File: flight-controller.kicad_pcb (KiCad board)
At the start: 2 copper layers, 51 x 54 mm, 32 parts, among them J1 XT60PW-M, J2 SM04B-SRSS-TB, J3 XT60PW-F, J4 XT60PW-F, J5 XT60PW-F, J6 XT60PW-F, U1 ACS773LCB-100B-PFF, U2 LMR33630ADDA, U3 AMS1117-3.3

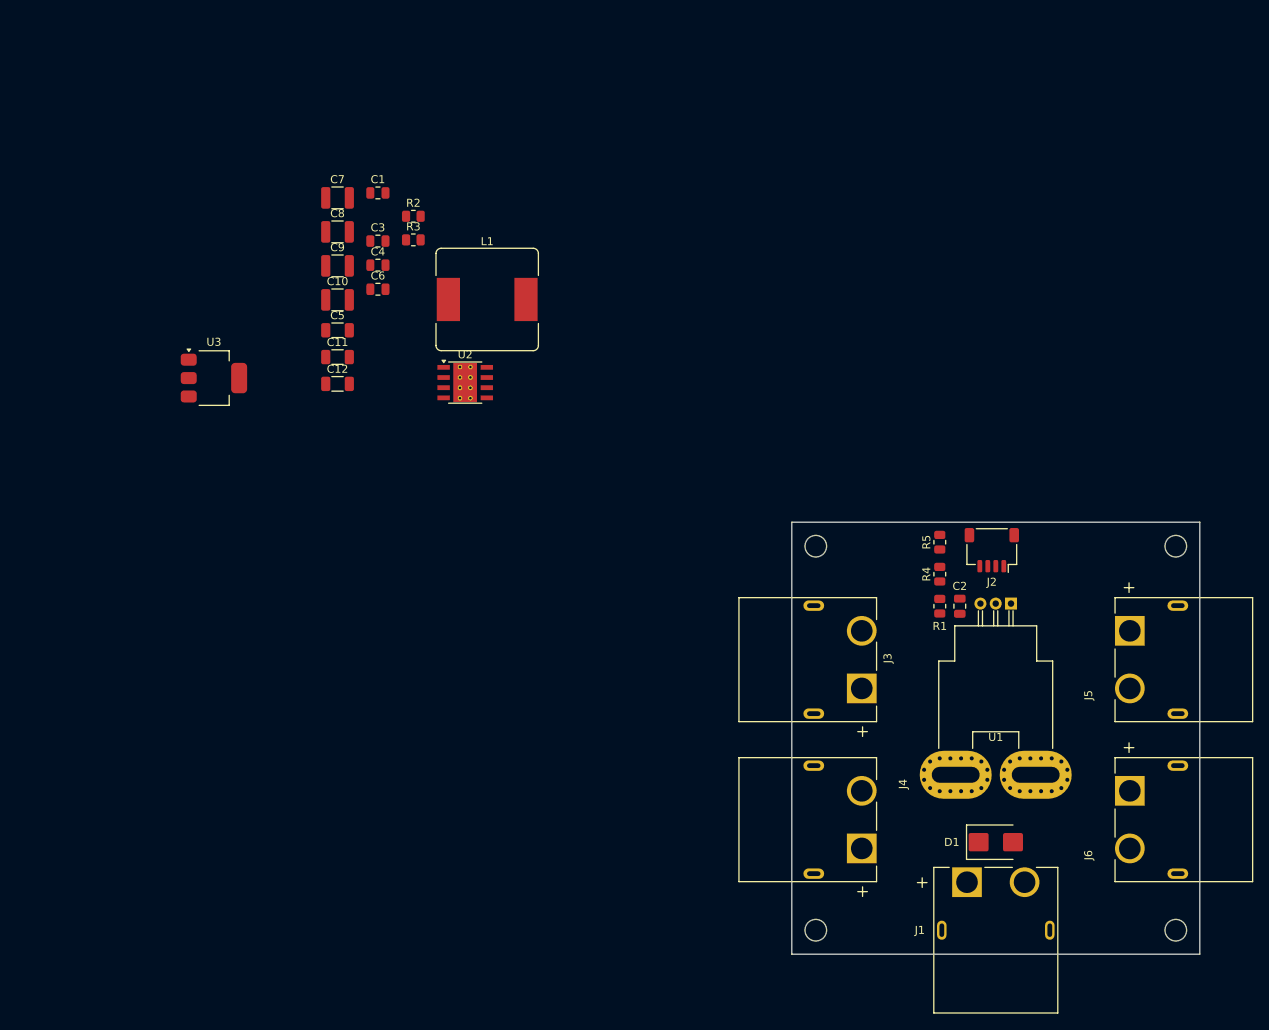
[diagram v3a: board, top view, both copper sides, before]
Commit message: feat: Placed buck converter
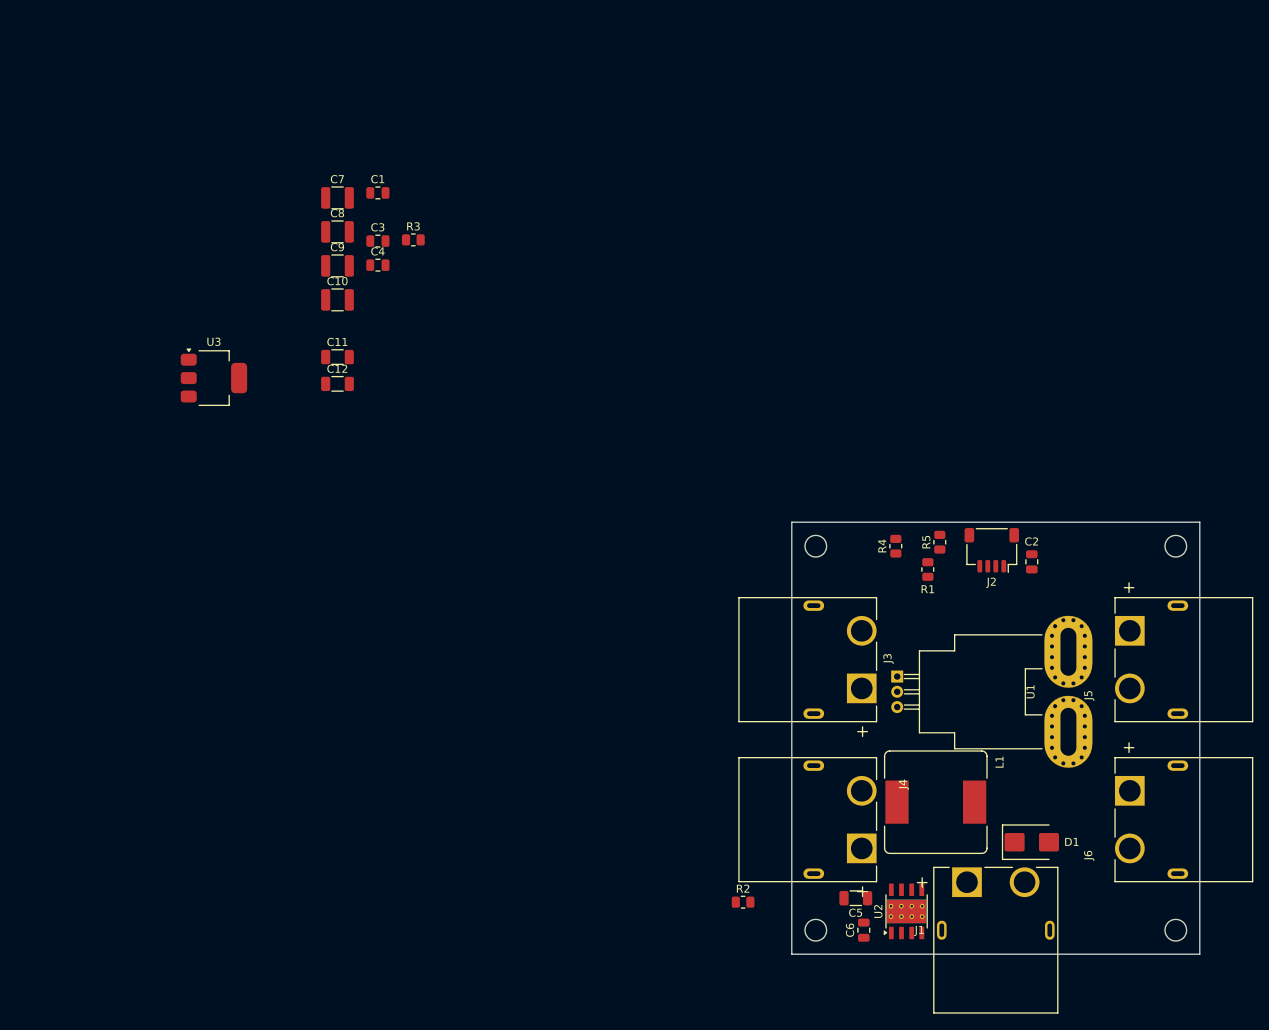
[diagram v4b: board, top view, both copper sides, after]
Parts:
- moved C6 100.5 mm to (123.0, 130.0), turned to 90 degrees
- moved C5 96.1 mm to (122.0, 126.0), turned to 180 degrees
- moved R2 95.1 mm to (107.9, 126.5)
- moved U2 86.1 mm to (128.3, 127.7), turned to 90 degrees
- moved L1 84.2 mm to (132.0, 114.0)
- moved U1 16.9 mm to (127.2, 98.3), turned to -90 degrees
- moved C2 10.6 mm to (144.0, 84.0)
- moved R4 6.52 mm to (127.0, 82.0)
- moved R1 4.83 mm to (131.0, 84.9)
- moved D1 4.50 mm to (144.0, 119.0)

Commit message: feat: Placed correct location buck converter
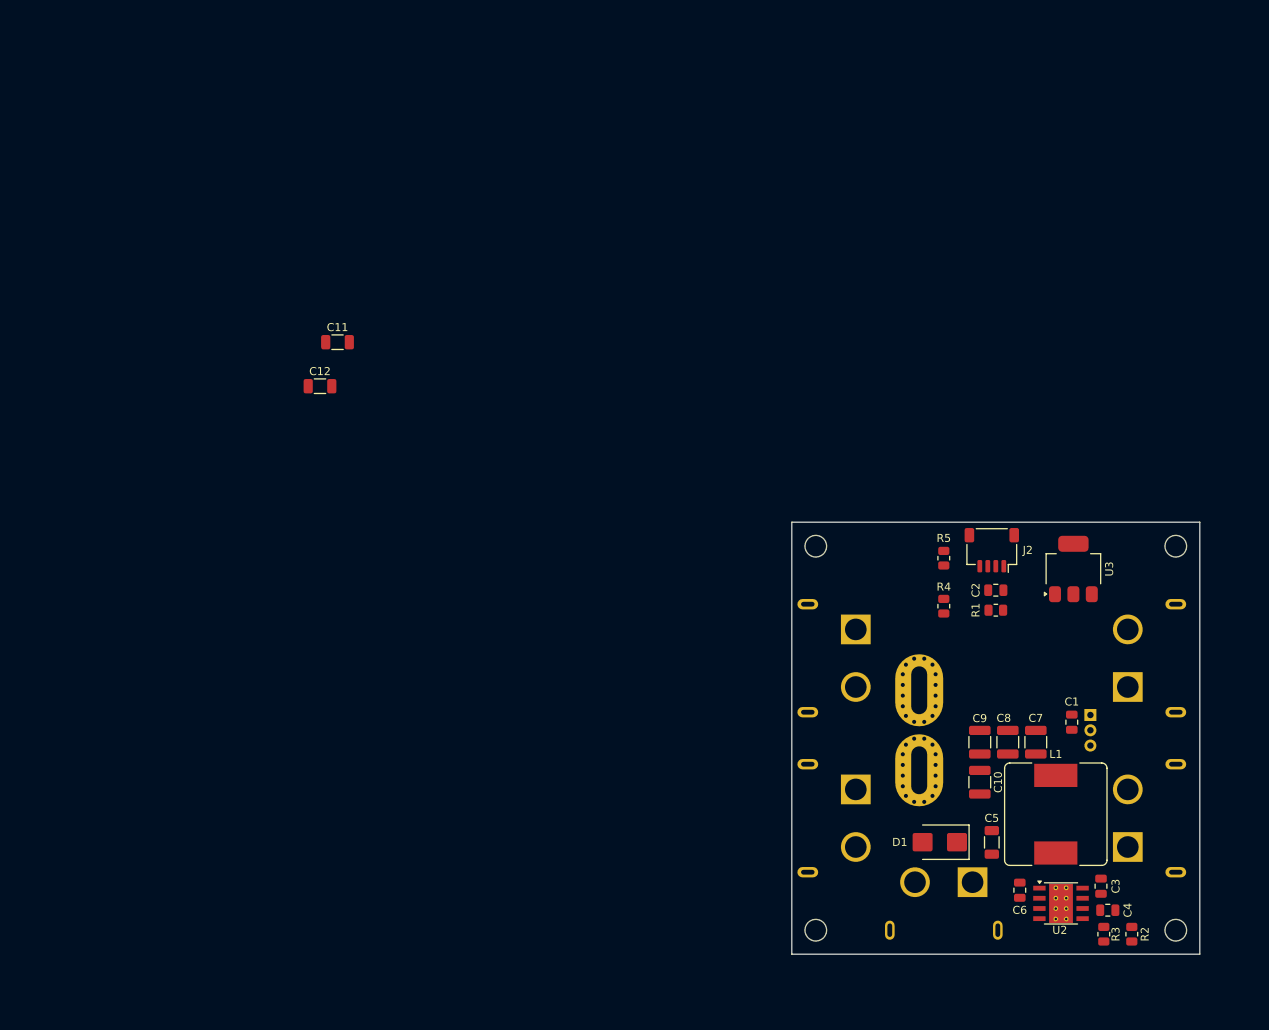
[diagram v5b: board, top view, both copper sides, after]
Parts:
- J1, J3, J4, J5, J6, U1: moved to B.Cu
- moved R3 122.4 mm to (153.0, 130.5), turned to -90 degrees
- moved C4 121.8 mm to (153.5, 127.5)
- moved C3 121.1 mm to (152.7, 124.5), turned to 90 degrees
- moved C7 110.7 mm to (144.5, 106.5), turned to 90 degrees
- moved U3 110.1 mm to (149.2, 84.8), turned to 90 degrees
- moved C1 109.1 mm to (149.0, 104.0), turned to -90 degrees
- moved C8 105.3 mm to (141.0, 106.5), turned to 90 degrees
- moved C10 100.4 mm to (137.5, 111.5), turned to -90 degrees
- moved C9 100.0 mm to (137.5, 106.5), turned to 90 degrees
- moved R2 48.8 mm to (156.5, 130.5), turned to -90 degrees
- moved U1 24.6 mm to (151.3, 103.1)
- moved C6 20.1 mm to (142.5, 125.0)
- moved U2 19.3 mm to (147.7, 126.7), turned to 0 degrees
- moved C5 18.4 mm to (139.0, 119.0), turned to 90 degrees
- moved L1 15.1 mm to (147.0, 115.5), turned to 90 degrees
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
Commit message: feat: Finished placing AMS
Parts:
- moved C11 96.9 mm to (148.5, 89.0)
- moved C12 91.8 mm to (144.5, 82.5), turned to 90 degrees
- moved C10 11.9 mm to (140.5, 100.0), turned to 90 degrees
- moved C9 9.19 mm to (144.0, 100.0)
- moved C2 5.02 mm to (134.5, 87.0)
- moved R1 5.02 mm to (134.5, 89.5)
- moved J2 5.00 mm to (134.0, 82.5)
- moved R4 4.61 mm to (128.5, 88.5)
- moved R5 4.50 mm to (128.5, 83.5)
- moved U3 1.55 mm to (150.5, 84.0), turned to 0 degrees
- moved C7 0.71 mm to (144.0, 106.0)
- moved C8 0.71 mm to (140.5, 106.0)
- moved C1 0.50 mm to (149.5, 104.0)
- moved U1 0.50 mm to (151.8, 103.1)

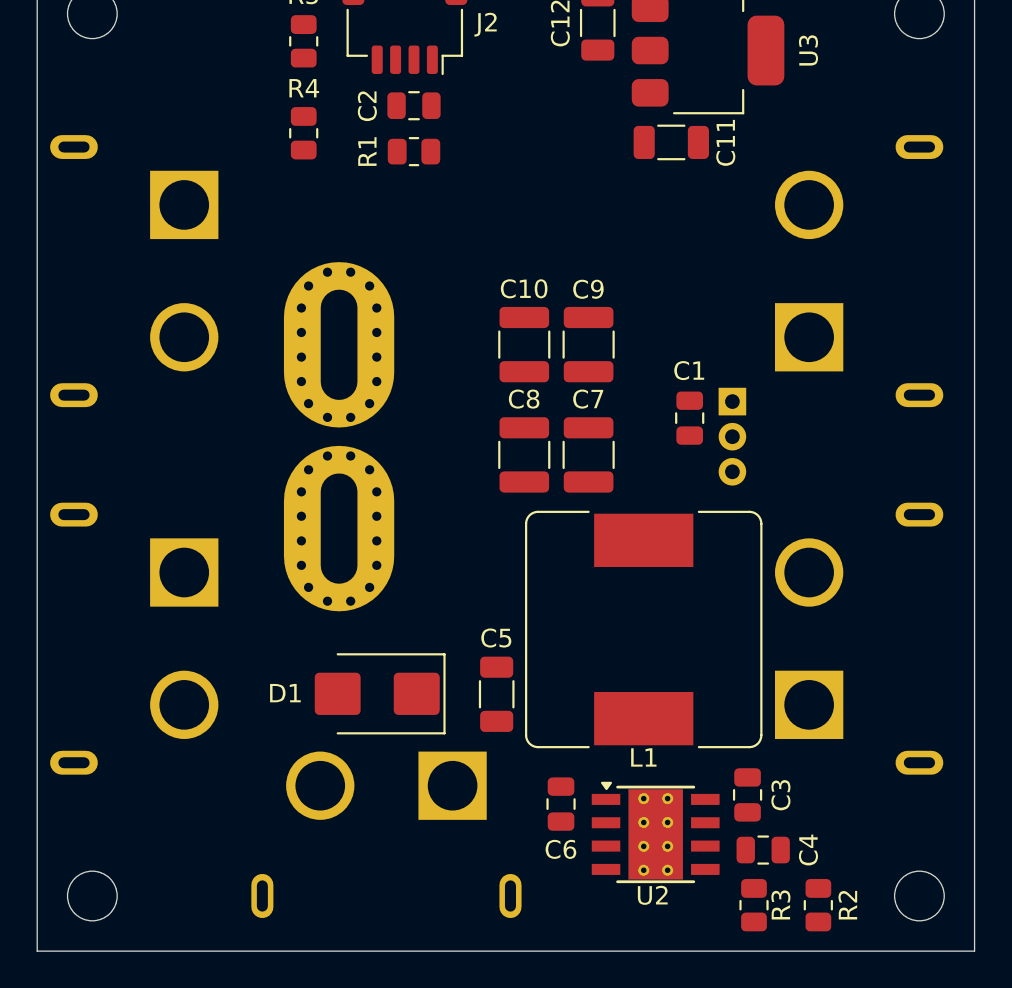
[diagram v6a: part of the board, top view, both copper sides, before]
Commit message: fix: Fixed DRC errors
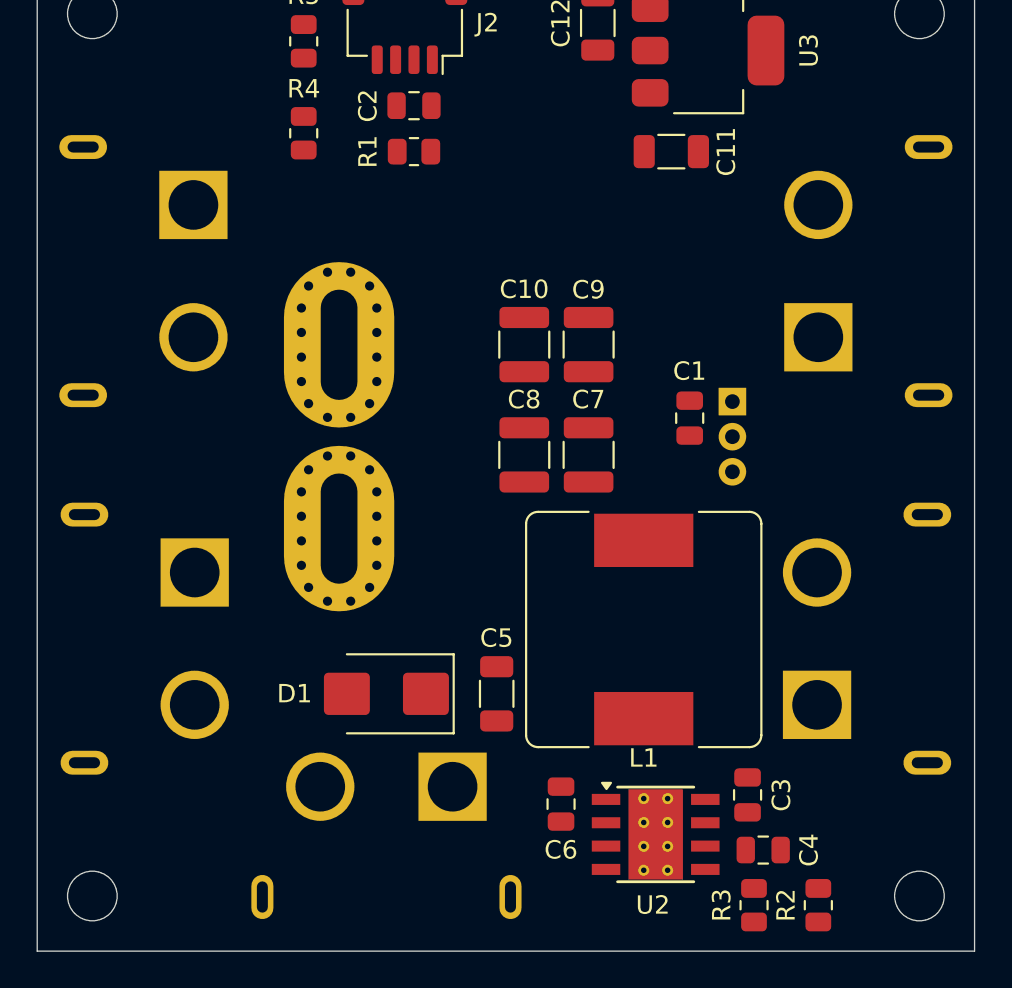
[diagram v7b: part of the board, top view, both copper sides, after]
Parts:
- moved J4 0.57 mm to (122.6, 116.0)
- moved C11 0.50 mm to (148.5, 89.5)
- moved D1 0.50 mm to (133.0, 119.0)
- moved J3 0.50 mm to (122.5, 96.0)
- moved J5 0.50 mm to (156.5, 96.0)
- moved J6 0.43 mm to (156.4, 116.0)
- moved J1 0.06 mm to (133.0, 130.1)
